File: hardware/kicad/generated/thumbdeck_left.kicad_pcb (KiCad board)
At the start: 4 copper layers, 76.5 x 114.5 mm, 85 parts, among them J2 FFC16, SW1 SNAP7, SW10 SNAP7, SW11 SNAP7, SW12 SNAP7, SW13 SNAP7, SW14 SNAP7, SW15 SNAP7, SW16 SNAP7, SW17 SNAP7, SW18 SNAP7, SW19 SNAP7, SW2 SNAP7, SW20 SNAP7, SW21 SNAP7, SW22 SNAP7, SW23 SNAP7, SW24 SNAP7, SW25 SNAP7, SW26 SNAP7, SW27 SNAP7, SW28 SNAP7, SW29 SNAP7, SW3 SNAP7, SW30 SNAP7, SW31 SNAP7, SW32 SNAP7, SW33 SNAP7, SW34 SNAP7, SW35 SNAP7, SW36 SNAP7, SW37 SNAP7, SW38 SNAP7, SW39 SNAP7, SW4 SNAP7, SW40 SNAP7, SW41 SNAP7, SW42 SNAP7, SW5 SNAP7, SW6 SNAP7, SW7 SNAP7, SW8 SNAP7, SW9 SNAP7

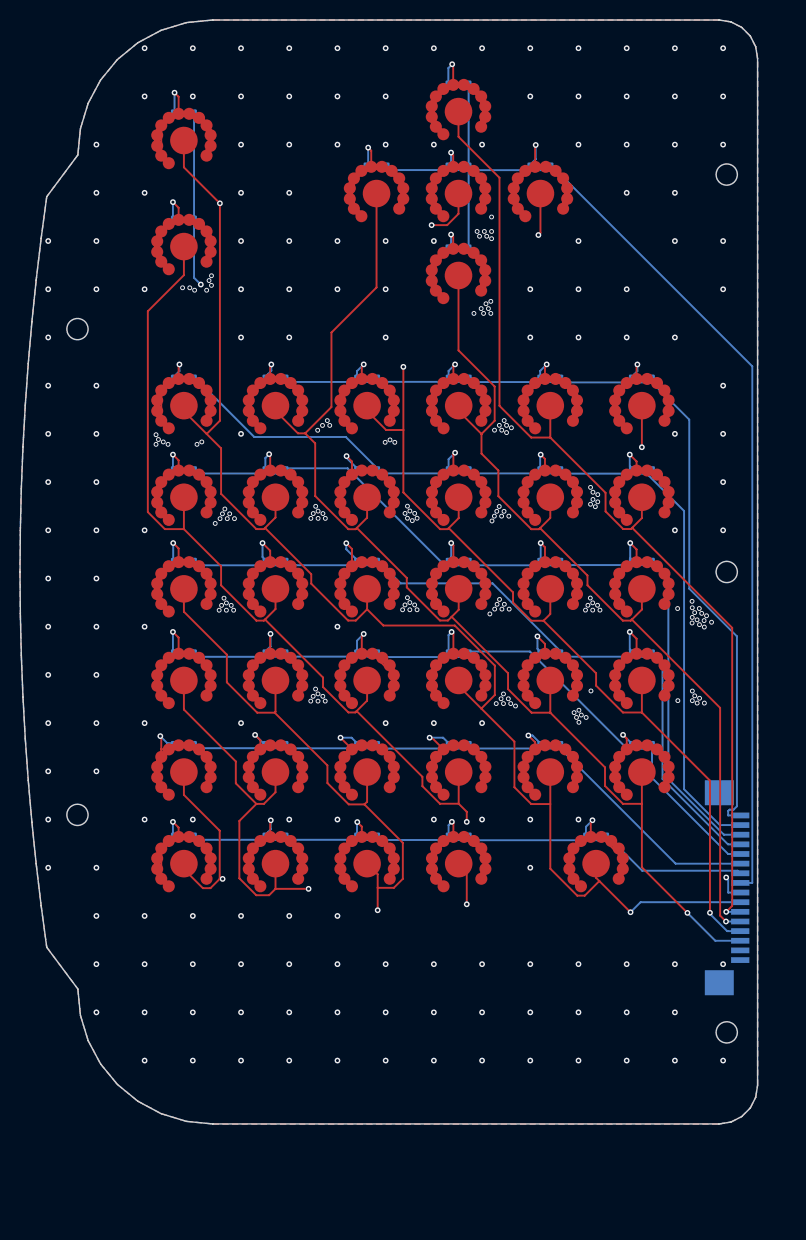
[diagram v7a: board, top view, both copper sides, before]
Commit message: v0.17: Rii-proportioned grips — chin cut, electronics to top, rectangular keys
Print-in-hand feedback on the right grip lid: the device towered over both the
phone (~80mm) and the Rii i8+ (~97mm) the layout mimics, with the excess in the
chin below the space row. This rev takes the grip 114.5 -> 97.0mm to match the
i8+, verified end-to-end.

PCB / 2D (both boards re-routed, 0 DRC violations / 0 unconnected):
- bottom_strip 19 -> 7: chin under the space row ~23 -> ~9mm
- rectangular keycaps 8.5 x 7.0 (2u space 18.5) at 10 x 9mm pitch (was 8x8 @ 9.5)
- E73 + entire power front-end relocated to the top zone (vacated trackpad space)
  as a rigid 180-deg rotation of the DRC-verified rev-A cluster (hand-routed USB
  copper carried along); antenna now UP off the centre-top edge; USB-C mouth +
  power-switch knob in the top wall; JST-PH in the chin; PgUp/PgDn inner-top
- top-outer corner sharpened r14 -> r10 (squarer i8+-like shoulders)
- fab package, firmware (byte-identical - matrix/pinmap unchanged) regenerated
- new verify_alignment.py: machine audit PCB<->model<->caps<->shell (all pass);
  switch re-evaluated and KEPT (Snaptron 7mm; sample light-force ~160-180gf)

3D (deck3d.py regenerated + fit-checked: 203 bodies, 0 collisions, all bed-fit):
- keymat plungers / lid openings now the real rounded-rect caps (cluster round)
- USB-C opening, switch slot, antenna wall relief moved to the top wall; knob
  direction derived from placed rotation; panel screws derived from pocket span
  (old y=105 floated off the 97mm shell)
- fixed latent v0.16 bug: cluster plungers were disconnected islands - web now
  grows the 3mm living-hinge strips the 2D concept drew + asserts connectivity
- fixed deck.product() origin rounding (0.003mm seam offset tripped frame assert)

Renders regenerated (2D + 3D); 15 obsolete orphan renders removed; docs + README
updated throughout.

Co-Authored-By: Claude Opus 4.8 (1M context) <noreply@anthropic.com>
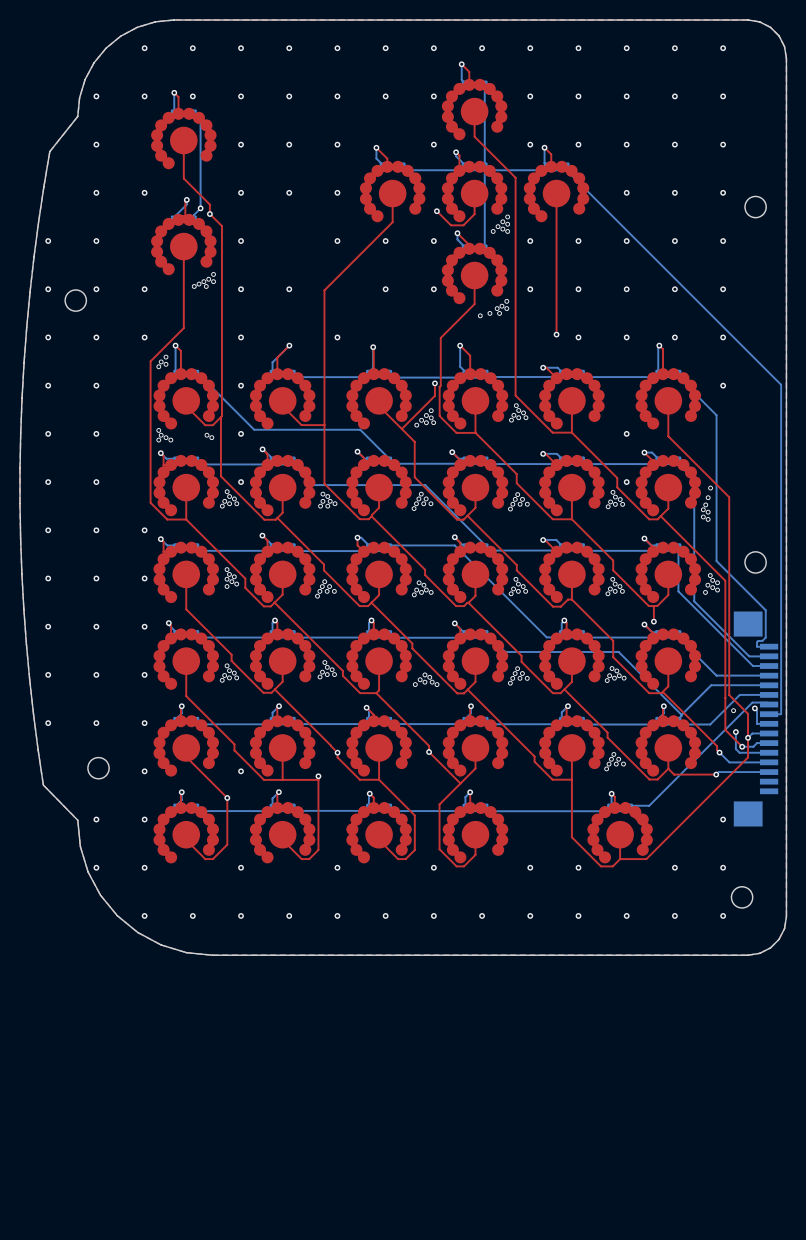
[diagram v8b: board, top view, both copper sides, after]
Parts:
- moved J2 17.8 mm to (75.9, 72.5)
- moved D31 3.90 mm to (62.2, 81.5)
- moved SW31 3.90 mm to (62.2, 84.5)
- moved D25 3.71 mm to (67.2, 72.5)
- moved SW25 3.71 mm to (67.2, 75.5)
- moved D32 3.47 mm to (47.2, 81.5)
- moved SW32 3.47 mm to (47.2, 84.5)
- moved D19 3.39 mm to (67.2, 63.5)
- moved SW19 3.39 mm to (67.2, 66.5)
- moved D26 3.36 mm to (57.2, 72.5)
- moved SW26 3.36 mm to (57.2, 75.5)
- moved D33 3.25 mm to (37.2, 81.5)
- moved SW33 3.25 mm to (37.2, 84.5)
- moved D13 3.13 mm to (67.2, 54.5)
- moved SW13 3.13 mm to (67.2, 57.5)
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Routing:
- net ROW7: track 119.1 -> 102.0 mm
- net COL7: track 187.3 -> 170.6 mm, vias 2 -> 3
- net ROW0: track 90.6 -> 75.7 mm
- net ROW2: track 86.5 -> 72.4 mm
- net ROW1: track 94.5 -> 80.5 mm
- net COL6: track 238.0 -> 224.8 mm, vias 3 -> 2
- net COL8: track 199.3 -> 186.2 mm
- net ROW8: track 105.2 -> 93.5 mm
- net ROW3: track 77.4 -> 66.9 mm
- net COL9: track 191.6 -> 182.1 mm
- net ROW6: track 60.1 -> 65.7 mm
- net DN_L5: track 16.9 -> 20.7 mm
- net DN_L3: track 16.9 -> 20.1 mm
- net ROW4: track 69.1 -> 66.2 mm
- net DN_L1: track 16.8 -> 19.7 mm
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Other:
- board size 76.5 x 114.5 mm -> 79.5 x 97 mm
